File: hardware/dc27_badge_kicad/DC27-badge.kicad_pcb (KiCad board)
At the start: 4 copper layers, 79.1 x 184.5 mm, 135 parts, among them J101 Conn_ARM_JTAG_SWD_10, J102 ShittyAddOnL, J103 ShittyAddOnR, J104 Conn_02x20_Odd_Even, J601 USB_MICRO_RIGHT, SW108 RESET, SW401 POWER ON, SW801 SKRHAAE010, SW802 SKRHAAE010, U100 BMD-340-A-R-DC27-peripheral-c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, U301 IS31FL3216A, U401 MCP73833, U402 LM1117-3.3, U501 CS4344-CZZ, U502 LM4880, U601 CP2102N-A01-GQFN28, U602 TPD3E001DRLR, Y101 32.768Khz XTAL

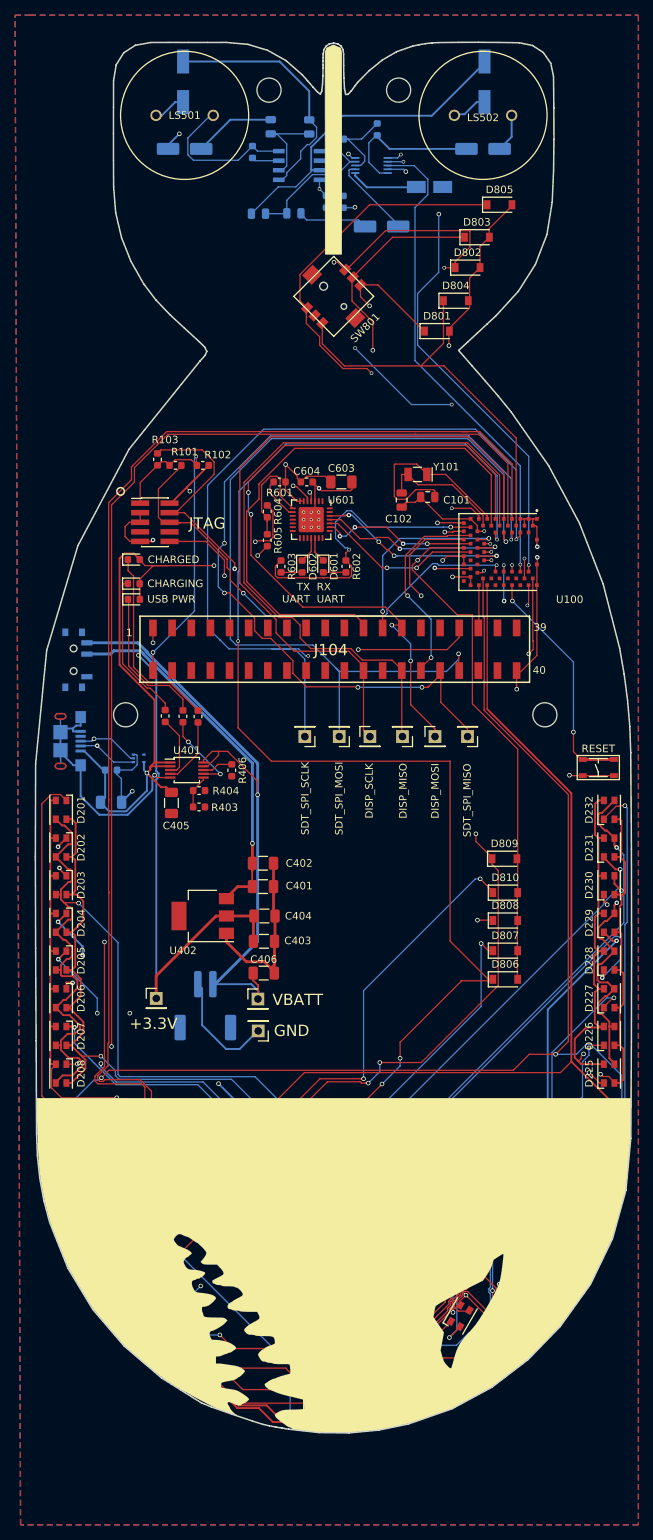
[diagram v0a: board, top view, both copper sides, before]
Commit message: add test points for DAC
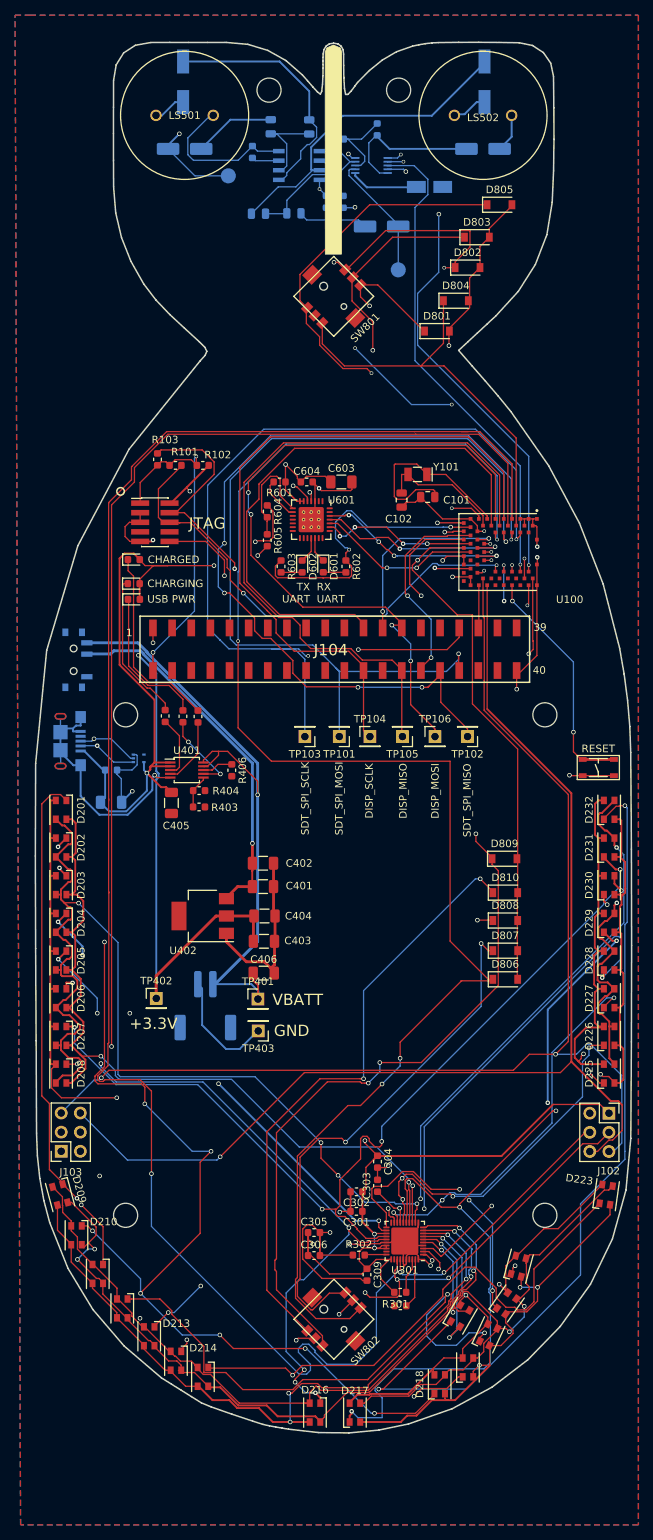
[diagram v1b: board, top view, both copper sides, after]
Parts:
- removed G***: LOGO, lib_fp:bombface-moved
- added TP501: DAC_OUT_R, TestPoint:TestPoint_Pad_D2.0mm, B.Cu at (91.2, 56.8)
- added TP502: DAC_OUT_L, TestPoint:TestPoint_Pad_D2.0mm, B.Cu at (113.8, 69.2)
- D201, D202, D203, D204, D205, D206, D207, D208, D209, D210, D211, D212, D213, D214, D215, D216, D217, D218, D219, D220, D221, D222, D223, D224, D225, D226, D227, D228, D229, D230, D231, D232: footprint lib_fp:LED_Cree-PLCC4_3.2x2.8mm_CCW -> LED_SMD:LED_Cree-PLCC4_3.2x2.8mm_CCW
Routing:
- net Net-(C504-Pad2): track 27.7 -> 37.1 mm
- net Net-(C506-Pad2): track 10.6 -> 16.3 mm

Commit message: check in charging circuit changes
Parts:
- added D404: SD0603S040S0R2, Diode_SMD:D_0603_1608Metric, F.Cu at (88.2, 145.4)
- added Q401: FDN360P, Package_TO_SOT_SMD:SOT-23, F.Cu at (91.7, 145.3)
- added R407: 10K, Resistor_SMD:R_0603_1608Metric, F.Cu at (84.0, 147.2)
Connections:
- SW401 pad 3: Net-(BT401-Pad1) -> Net-(D404-Pad1)
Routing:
- net Net-(D404-Pad1): track 0.00 -> 47.2 mm, vias 0 -> 1
- net Net-(BT401-Pad1): track 87.8 -> 61.2 mm, vias 1 -> 0
- net VBUS: track 94.8 -> 117.1 mm
- net GND: track 271.2 -> 280.7 mm
- net SW4: track 76.6 -> 78.0 mm
- net SW6: track 70.6 -> 72.0 mm
- net SW5: track 83.6 -> 84.2 mm

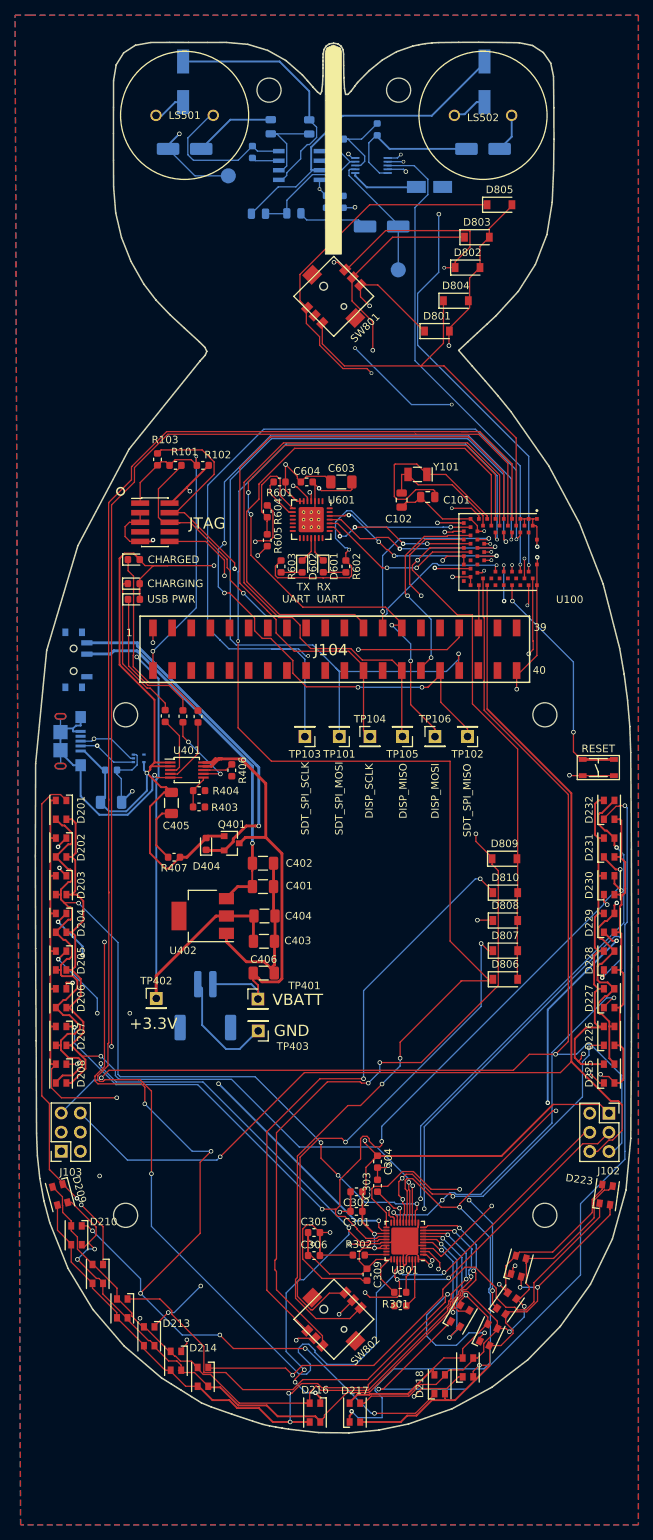
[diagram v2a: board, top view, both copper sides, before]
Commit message: add test points for the DAC. Add new context secret codes
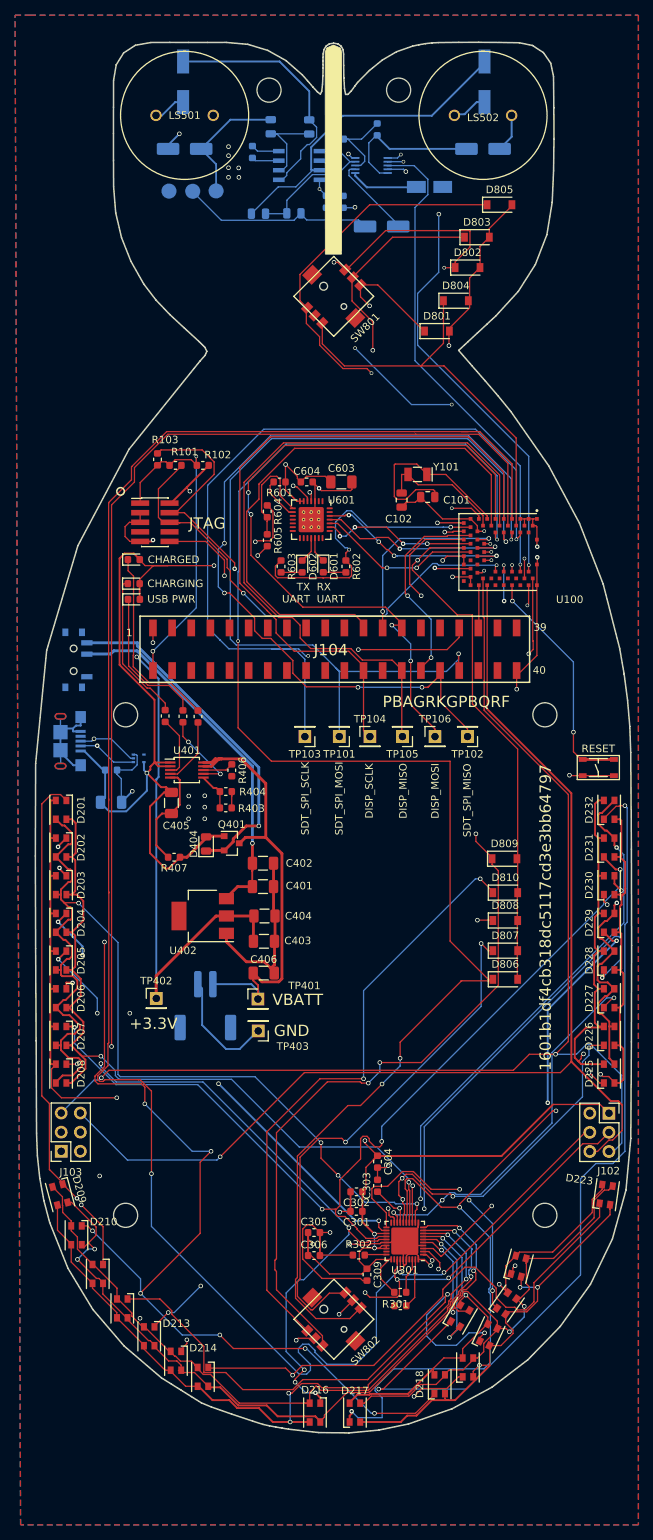
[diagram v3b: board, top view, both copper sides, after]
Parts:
- added TP503: DAC_GND, TestPoint:TestPoint_Pad_D2.0mm, B.Cu at (83.3, 58.8)
- D404: value SD0603S040S0R2 -> SD0805S020S1R0; footprint Diode_SMD:D_0603_1608Metric -> Diode_SMD:D_0805_2012Metric
- moved TP502 29.2 mm to (86.5, 58.8)
- moved R403 3.55 mm to (90.9, 140.7)
- moved R404 3.55 mm to (90.9, 138.5)
- moved TP501 2.58 mm to (89.6, 58.8)
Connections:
- TP501 pad 1: Net-(C504-Pad2) -> Net-(C504-Pad1)
- TP502 pad 1: Net-(C506-Pad2) -> Net-(C506-Pad1)
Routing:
- net GND: track 280.7 -> 251.1 mm, vias 20 -> 31
- net Net-(C506-Pad1): track 9.34 -> 25.7 mm
- net Net-(C504-Pad2): track 37.1 -> 27.7 mm
- net Net-(C504-Pad1): track 10.6 -> 17.0 mm
- net Net-(C506-Pad2): track 16.3 -> 10.6 mm
- net CS8: track 207.3 -> 208.6 mm
- net Net-(R403-Pad1): track 4.21 -> 5.19 mm
- net VBUS: track 117.1 -> 116.6 mm
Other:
- board text added: "1601b1df4cb318dc5117cd3e3bb64797"
- board text added: "32c850"
- board text added: "PBAGRKGPBQRF"
- board text added: "da Bomb! DEF CON 27 (2019) John Adams, Bill Paul, Egan Hirvela https://teamides.com https://github.com/netik/dc27_badge Sponsored by New Context https://www.newcontext.com Powered by ChibiOS greets to everyone living #badgelife"

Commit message: forgot to check in and add bomb-face to the mechanicals schematic and pcb
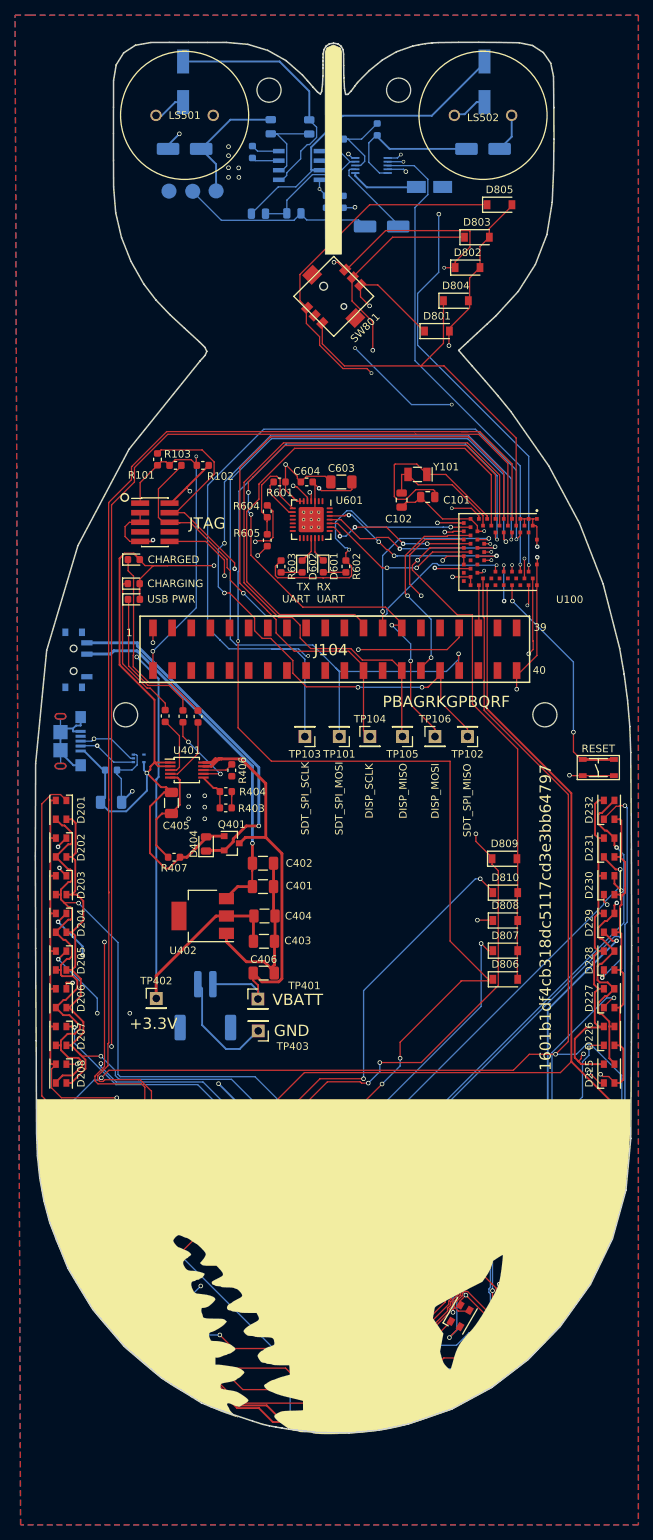
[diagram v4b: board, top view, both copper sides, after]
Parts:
- added H701: MountingHole-Mechanical, lib_fp:bombface-moved, F.Cu at (105.2, 201.5)

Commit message: update schematic and re-check in gerbers
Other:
- board text added: "da Bomb! - rev3 DEF CON 27 (2019) John Adams, Bill Paul, Egan Hirvela https://teamides.com https://github.com/netik/dc27_badge Sponsored by New Context https://www.newcontext.com Powered by ChibiOS http://www.chbios.org greets to everyone living #badgelife"
- board text removed: "da Bomb! DEF CON 27 (2019) John Adams, Bill Paul, Egan Hirvela https://teamides.com https://github.com/netik/dc27_badge Sponsored by New Context https://www.newcontext.com Powered by ChibiOS greets to everyone living #badgelife"
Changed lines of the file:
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@@
     (aux_axis_origin 0 0)
     (grid_origin 104.15 65.4)
-    (visible_elements FFFFFF7F)
+    (visible_elements FFFFEF7F)
     (pcbplotparams
       (layerselection 0x010fc_ffffffff)
@@
       (drillshape 0)
       (scaleselection 1)
-      (outputdirectory "gerbers/PROTO_V2/"))
+      (outputdirectory "gerbers/FINAL/"))
   )
   (net 0 "")
@@
     )
   )
-  (gr_text "da Bomb!\nDEF CON 27 (2019)\nJohn Adams, Bill Paul, Egan Hirvela\nhttps://teamides.com\nhttps://github.com/netik/dc27_badge\n\nSponsored by New Context\nhttps://www.newcontext.com\n\nPowered by ChibiOS\ngreets to everyone living #badgelife\n" (at 105.15 80.075 90) (layer B.SilkS)
+  (gr_text "da Bomb! - rev3\nDEF CON 27 (2019)\nJohn Adams, Bill Paul, Egan Hirvela\nhttps://teamides.com\nhttps://github.com/netik/dc27_badge\n\nSponsored by New Context\nhttps://www.newcontext.com\n\nPowered by ChibiOS\nhttp://www.chbios.org\n\ngreets to everyone living #badgelife\n" (at 104.925 80.675 90) (layer B.SilkS)
     (effects (font (size 1.5 1.5) (thickness 0.3)) (justify left mirror))
   )
@@
   (segment (start 96.83 49.325) (end 91.475 49.325) (width 0.254) (layer B.Cu) (net 53) (status 10))
   (segment (start 91.475 49.325) (end 87.8 53) (width 0.254) (layer B.Cu) (net 53) (status 20))
-  (segment (start 89.575 58.775) (end 89.575 55.225) (width 0.254) (layer B.Cu) (net 53))
-  (segment (start 89.575 55.225) (end 87.525 53.175) (width 0.254) (layer B.Cu) (net 53))
+  (segment (start 89.575 58.775) (end 89.575 55.225) (width 0.254) (layer B.Cu) (net 53) (status 10))
+  (segment (start 89.575 55.225) (end 87.525 53.175) (width 0.254) (layer B.Cu) (net 53) (status 20))
   (segment (start 96.37 102.625) (end 96.34 102.655) (width 0.1524) (layer F.Cu) (net 54))
   (segment (start 96.37 102.0875) (end 96.37 102.625) (width 0.1524) (layer F.Cu) (net 54) (status 10))
@@
   (segment (start 101.60929 62.62929) (end 100.82 61.84) (width 0.1524) (layer B.Cu) (net 61) (status 20))
   (segment (start 99.91129 62.67621) (end 90.27621 62.67621) (width 0.1524) (layer B.Cu) (net 61))
-  (segment (start 100.8375 61.75) (end 99.91129 62.67621) (width 0.1524) (layer B.Cu) (net 61))
-  (segment (start 90.27621 62.67621) (end 86.475 58.875) (width 0.1524) (layer B.Cu) (net 61))
+  (segment (start 100.8375 61.75) (end 99.91129 62.67621) (width 0.1524) (layer B.Cu) (net 61) (status 10))
+  (segment (start 90.27621 62.67621) (end 86.475 58.875) (width 0.1524) (layer B.Cu) (net 61) (status 20))
   (segment (start 98.9125 61.8) (end 98.9625 61.75) (width 0.1524) (layer B.Cu) (net 62) (status 30))
   (segment (start 96.1375 61.8) (end 98.9125 61.8) (width 0.1524) (layer B.Cu) (net 62) (status 30))
